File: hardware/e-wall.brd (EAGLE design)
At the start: 100 x 80 mm, 20 parts, among them IC1 74HCT595N, IC2 74HCT595N, IC3 74HCT595N, IC4 ULN2803, IC5 ULN2803, IC6 ULN2803, T1 BC547, T2 BC557, T3 BC547

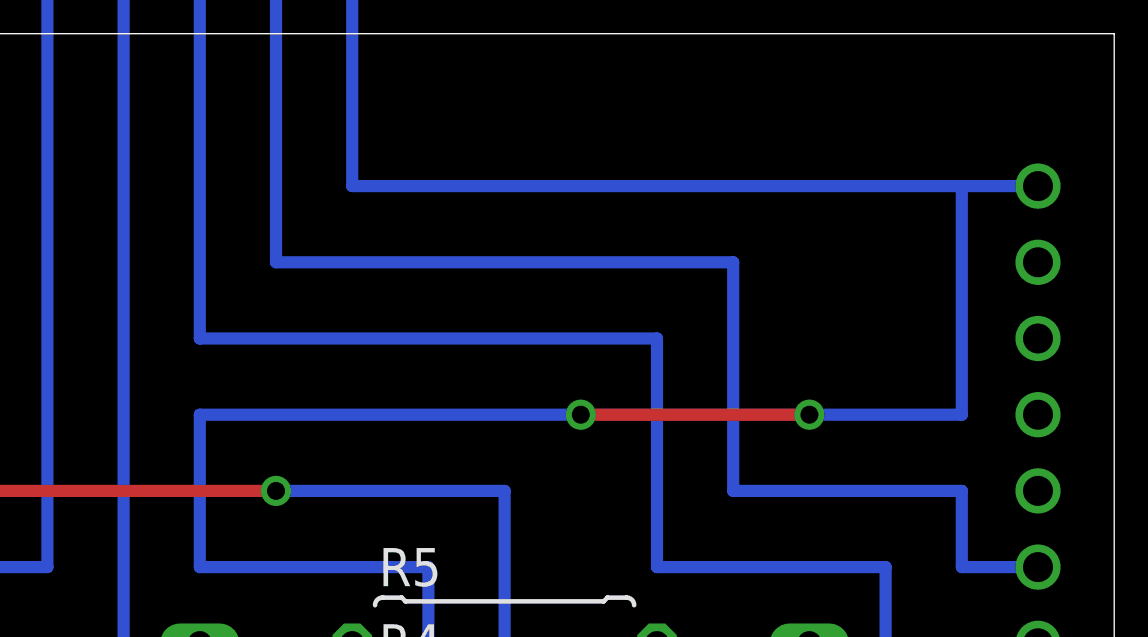
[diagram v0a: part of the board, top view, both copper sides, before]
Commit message: Spannungsteiler für SOMI
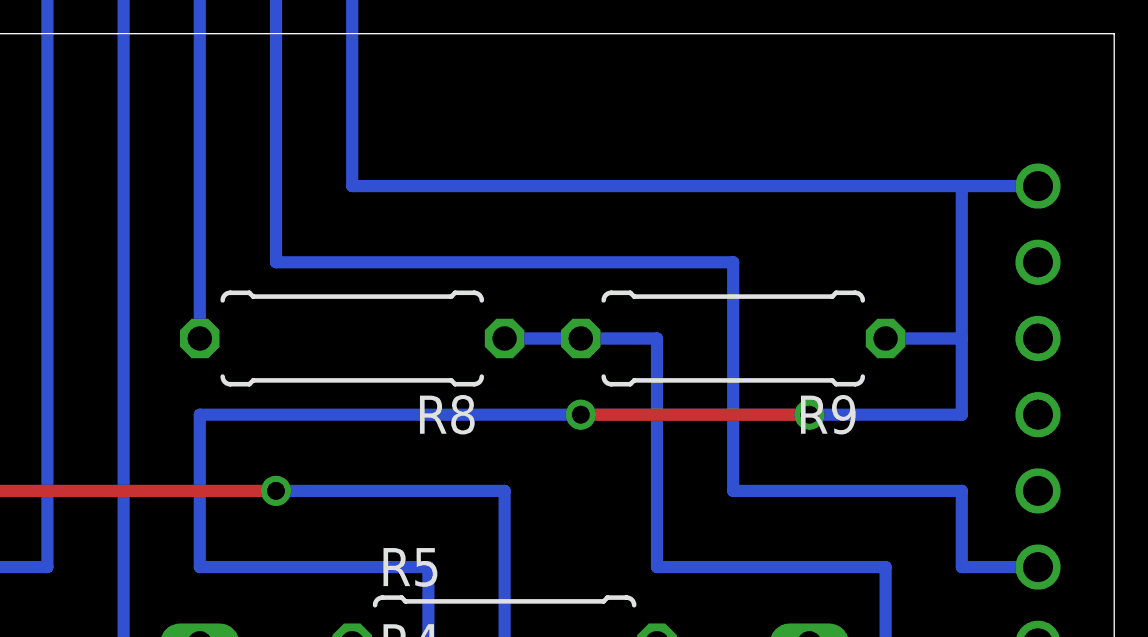
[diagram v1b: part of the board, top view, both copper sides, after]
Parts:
- added R8: 20k, resistor:0309/10
- added R9: 30k, resistor:0309/10
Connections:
- new net N$28: R8.1, R9.2, U$1.14
- net GND: now also R9.1
- net SOMI: now also R8.2; no longer U$1.14
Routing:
- net SOMI: track 132.1 -> 94.0 mm
- net N$28: track 0.00 -> 27.9 mm
- net GND: track 419.1 -> 421.6 mm
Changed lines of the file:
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@@
 <element name="IC5" library="uln-udn" package="DIL18" value="ULN2803" x="87.63" y="35.56" rot="R270"/>
 <element name="IC6" library="uln-udn" package="DIL18" value="ULN2803" x="87.63" y="58.42" rot="R270"/>
+<element name="R8" library="resistor" package="0309/10" value="20k" x="25.4" y="30.48" rot="R180"/>
+<element name="R9" library="resistor" package="0309/10" value="30k" x="38.1" y="30.48" rot="R180"/>
 </elements>
 <signals>
@@
 <via x="40.64" y="27.94" extent="1-16" drill="0.6"/>
 <wire x1="40.64" y1="27.94" x2="45.72" y2="27.94" width="0.4064" layer="16"/>
-<wire x1="45.72" y1="27.94" x2="45.72" y2="35.56" width="0.4064" layer="16"/>
+<wire x1="45.72" y1="27.94" x2="45.72" y2="30.48" width="0.4064" layer="16"/>
+<wire x1="45.72" y1="30.48" x2="45.72" y2="35.56" width="0.4064" layer="16"/>
 <wire x1="45.72" y1="35.56" x2="48.26" y2="35.56" width="0.4064" layer="16"/>
 <wire x1="55.88" y1="66.04" x2="25.4" y2="66.04" width="0.4064" layer="16"/>
 <wire x1="25.4" y1="66.04" x2="25.4" y2="35.56" width="0.4064" layer="16"/>
 <wire x1="25.4" y1="35.56" x2="45.72" y2="35.56" width="0.4064" layer="16"/>
+<contactref element="R9" pad="1"/>
+<wire x1="43.18" y1="30.48" x2="45.72" y2="30.48" width="0.4064" layer="16"/>
 </signal>
 <signal name="VCC">
@@
 <signal name="SOMI">
 <contactref element="IC3" pad="9"/>
-<contactref element="U$1" pad="14"/>
 <wire x1="73.66" y1="71.12" x2="71.12" y2="71.12" width="0.4064" layer="16"/>
 <via x="71.12" y="71.12" extent="1-16" drill="0.6"/>
@@
 <wire x1="58.42" y1="71.12" x2="20.32" y2="71.12" width="0.4064" layer="16"/>
 <wire x1="20.32" y1="71.12" x2="20.32" y2="30.48" width="0.4064" layer="16"/>
-<wire x1="20.32" y1="30.48" x2="35.56" y2="30.48" width="0.4064" layer="16"/>
-<wire x1="35.56" y1="30.48" x2="35.56" y2="22.86" width="0.4064" layer="16"/>
-<wire x1="35.56" y1="22.86" x2="43.18" y2="22.86" width="0.4064" layer="16"/>
-<wire x1="43.18" y1="22.86" x2="43.18" y2="20.32" width="0.4064" layer="16"/>
-<wire x1="43.18" y1="20.32" x2="48.26" y2="20.32" width="0.4064" layer="16"/>
+<contactref element="R8" pad="2"/>
 </signal>
 <signal name="OUT0">
@@
 <wire x1="91.44" y1="5.08" x2="93.98" y2="5.08" width="0.4064" layer="16"/>
 </signal>
+<signal name="N$28">
+<contactref element="U$1" pad="14"/>
+<contactref element="R9" pad="2"/>
+<contactref element="R8" pad="1"/>
+<wire x1="30.48" y1="30.48" x2="33.02" y2="30.48" width="0.4064" layer="16"/>
+<wire x1="33.02" y1="30.48" x2="35.56" y2="30.48" width="0.4064" layer="16"/>
+<wire x1="35.56" y1="30.48" x2="35.56" y2="22.86" width="0.4064" layer="16"/>
+<wire x1="35.56" y1="22.86" x2="43.18" y2="22.86" width="0.4064" layer="16"/>
+<wire x1="43.18" y1="22.86" x2="43.18" y2="20.32" width="0.4064" layer="16"/>
+<wire x1="43.18" y1="20.32" x2="48.26" y2="20.32" width="0.4064" layer="16"/>
+</signal>
 </signals>

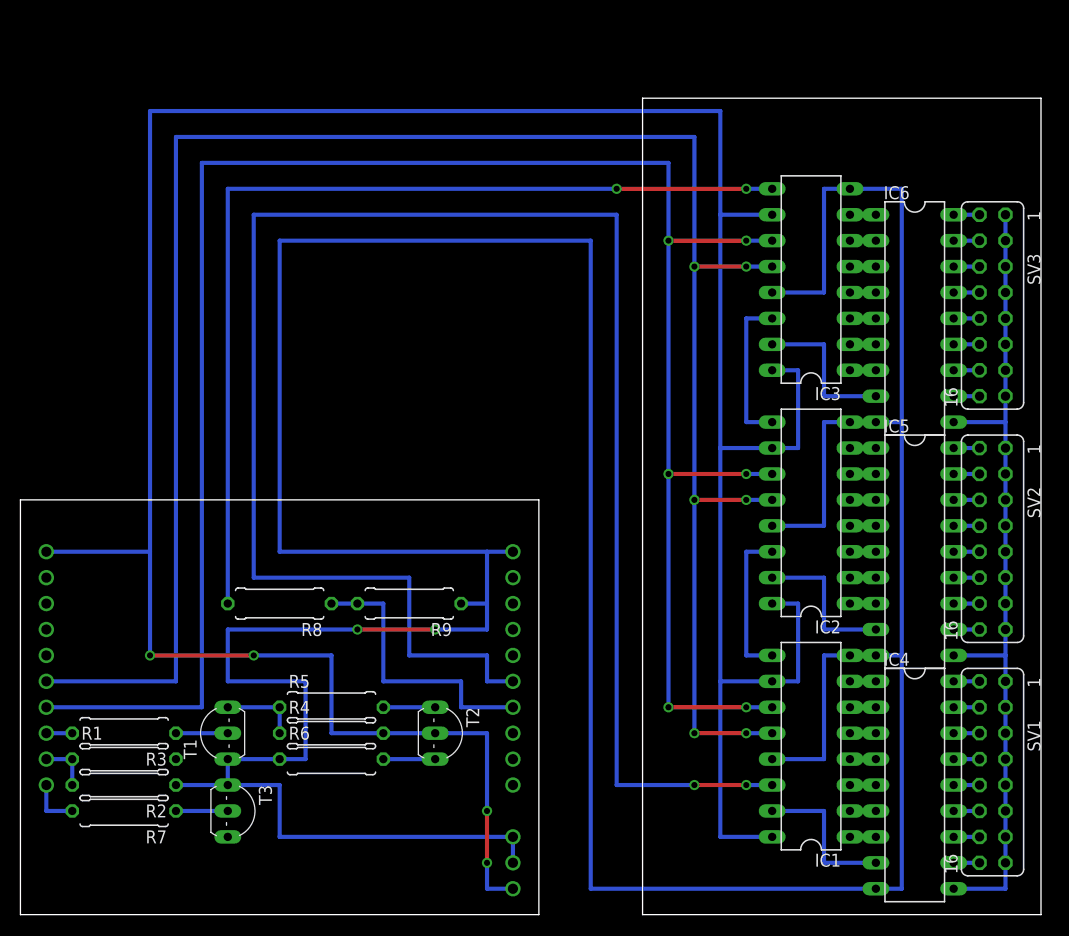
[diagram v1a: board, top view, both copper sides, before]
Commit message: Ultraschallsensor eingebaut
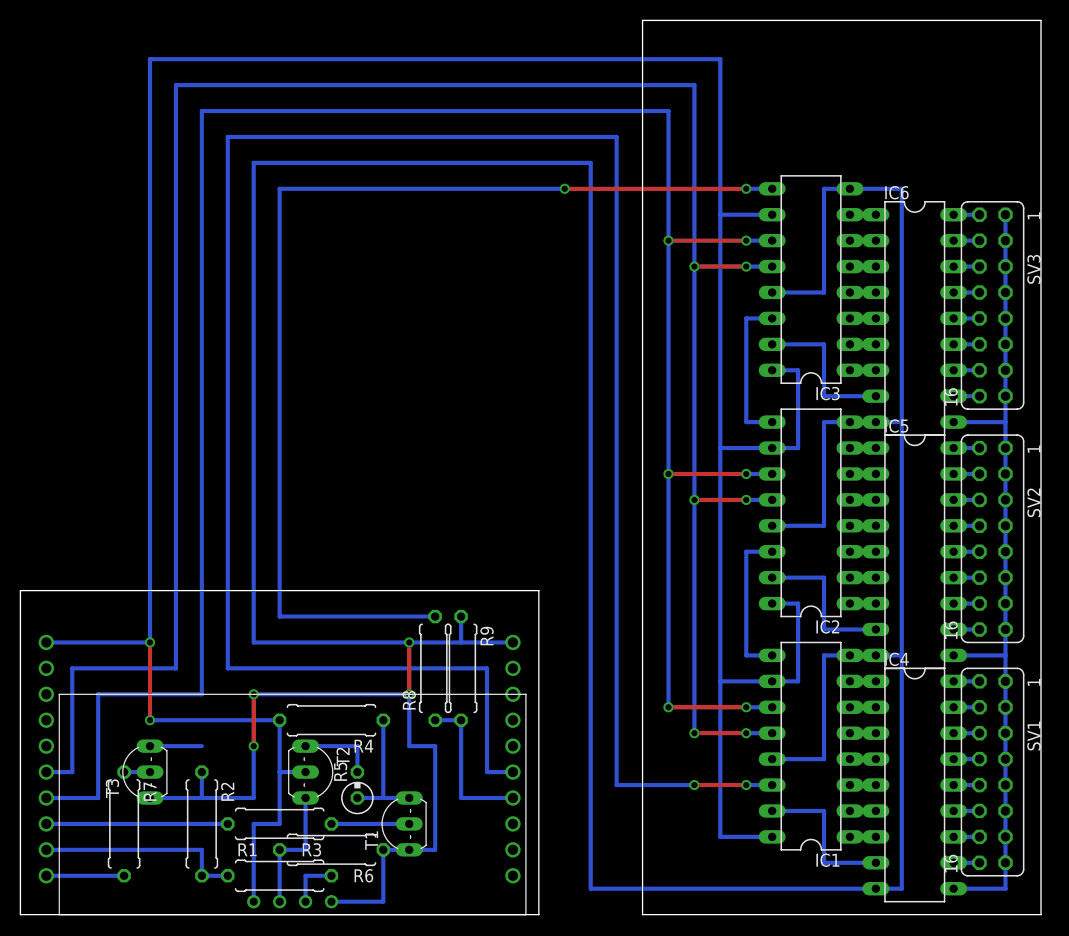
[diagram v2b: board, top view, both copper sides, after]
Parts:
- added U$2: (no value), ultrasonic:HC-SR04
- R5: device resistor:0309/10 -> resistor:0309V
- U$1: value Launchpad -> (none); device msp430launchpad:MSP430LAUNCHPAD_FULL -> msp430launchpad:MSP430LAUNCHPAD_BASIC
- moved T1 19.9 mm to (36.8, 8.89)
- moved R1 19.0 mm to (25.4, 3.81)
- moved R3 17.6 mm to (25.4, 8.89)
- moved R8 16.5 mm to (40.6, 24.1), turned to 90 degrees
- moved T2 13.3 mm to (27.9, 14.0)
- moved T3 10.9 mm to (11.4, 14.0), turned to 90 degrees
- moved R6 8.89 mm to (30.5, 6.35), turned to 180 degrees
- moved U$1 8.89 mm to (25.4, 15.2)
- moved R2 8.52 mm to (17.8, 8.89), turned to 270 degrees
- moved R9 8.13 mm to (43.2, 24.1), turned to 270 degrees
- moved R5 8.03 mm to (33.0, 12.7), turned to 90 degrees
- moved R4 1.27 mm to (30.5, 19.1), turned to 180 degrees
- moved R7 1.27 mm to (10.2, 8.89), turned to 270 degrees
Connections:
- net ECHO: now also U$2.P$3
- net GND: now also U$2.P$4; no longer U$1.22, U$1.23
- net TRIGGER: now also U$2.P$2
- net VCC: now also U$2.P$1; no longer U$1.21
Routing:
- net SIMO: track 177.8 -> 207.0 mm
- net EN: track 198.1 -> 217.2 mm
- net CLK: track 198.1 -> 217.2 mm
- net TRIGGER_UC: track 2.54 -> 17.8 mm
- net ECHO_UC: track 5.08 -> 20.3 mm
- net N$28: track 27.9 -> 15.2 mm
- net SOMI: track 94.0 -> 105.4 mm
- net TRIGGER: track 5.08 -> 12.7 mm
- net VCC: track 294.6 -> 288.3 mm, vias 4 -> 2
- net POWER_ON: track 0.00 -> 5.08 mm
- net N$34: track 7.62 -> 12.7 mm
- net ECHO: track 0.00 -> 5.08 mm
- net N$35: track 5.08 -> 7.62 mm
- net N$37: track 5.08 -> 7.62 mm
- net N$36: track 5.08 -> 2.54 mm
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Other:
- board size 100 x 80 mm -> 100 x 87.6 mm

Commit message: Package der Widerstände geändert
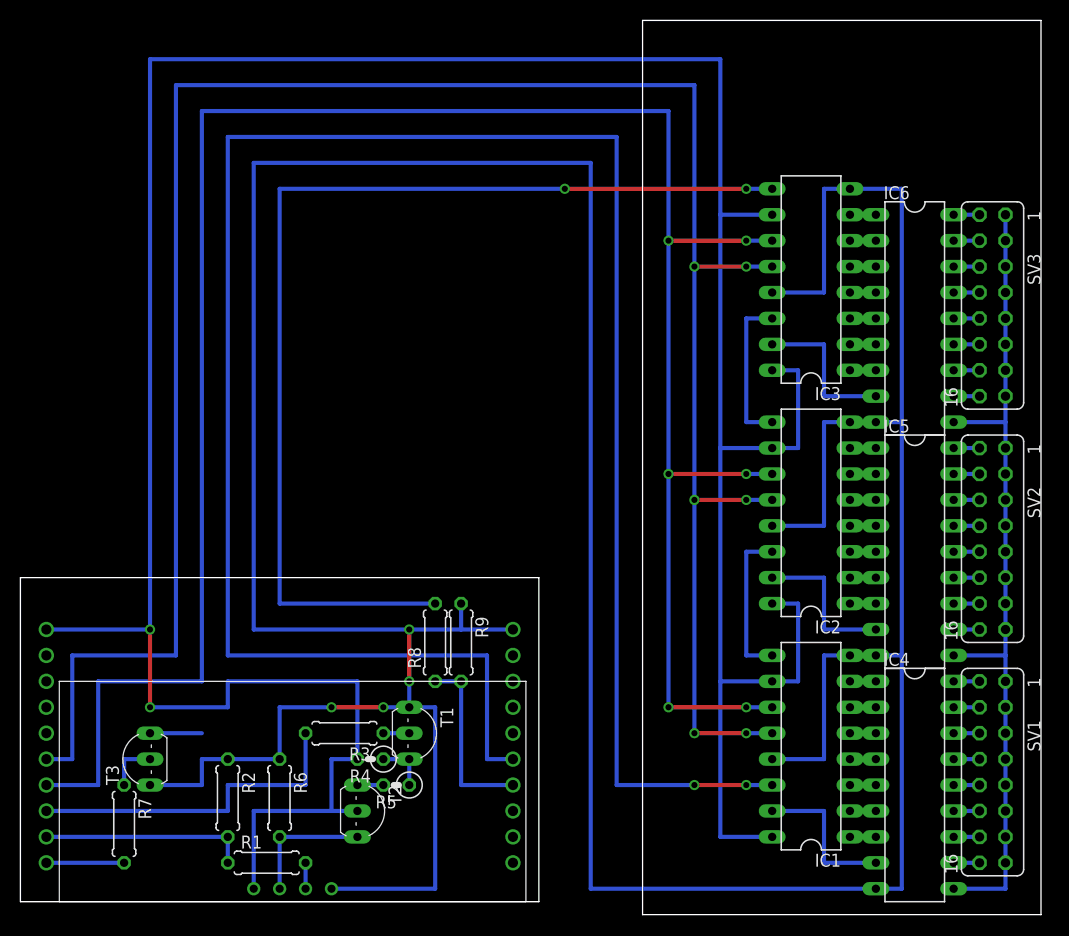
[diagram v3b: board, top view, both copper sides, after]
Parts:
- R1, R2, R3, R6, R7, R8, R9: device resistor:0309/10 -> resistor:0207/7
- R4: device resistor:0309/10 -> resistor:0207/2V
- R5: device resistor:0309V -> resistor:0207/2V
- moved R3 10.9 mm to (31.8, 17.8)
- moved T1 9.25 mm to (39.4, 17.8), turned to 270 degrees
- moved R6 7.18 mm to (25.4, 11.4), turned to 270 degrees
- moved T2 6.35 mm to (33.0, 10.2)
- moved R4 5.39 mm to (34.3, 15.2)
- moved R5 3.81 mm to (36.8, 12.7), turned to 180 degrees
- moved R2 3.59 mm to (20.3, 11.4)
- moved R8 2.54 mm to (40.6, 26.7)
- moved R9 2.54 mm to (43.2, 26.7)
- moved R1 1.80 mm to (24.1, 5.08)
- moved U$1 1.27 mm to (25.4, 16.5)
- moved U$2 1.27 mm to (26.7, 2.54)
- moved T3 1.27 mm to (11.4, 15.2)
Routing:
- net VCC: track 288.3 -> 307.3 mm
- net TRIGGER_UC: track 17.8 -> 33.0 mm
- net N$34: track 12.7 -> 5.08 mm
- net GND: track 422.9 -> 416.6 mm
- net N$35: track 7.62 -> 2.54 mm
- net N$33: track 7.62 -> 2.54 mm
- net N$36: track 2.54 -> 5.08 mm
- net N$28: track 15.2 -> 17.8 mm
- net ECHO: track 5.08 -> 2.54 mm
- net SIMO: track 207.0 -> 205.7 mm
- net SOMI: track 105.4 -> 104.1 mm
- net EN: track 217.2 -> 215.9 mm
- net CLK: track 217.2 -> 215.9 mm
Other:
- outline, holes or cut-outs redrawn

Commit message: Leitungen für SPI umbenannt
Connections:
- net N$28 renamed SOMI_UC
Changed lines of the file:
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@@
 <wire x1="91.44" y1="5.08" x2="93.98" y2="5.08" width="0.4064" layer="16"/>
 </signal>
-<signal name="N$28">
+<signal name="SOMI_UC">
 <contactref element="R9" pad="2"/>
 <contactref element="R8" pad="1"/>
@@
 </signal>
 </signals>
-<errors>
-</errors>
 </board>
 </drawing>
